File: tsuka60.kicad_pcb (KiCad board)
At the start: 2 copper layers, 285 x 95.1 mm, 166 parts, among them SW1 SW_Push, U1 ATmega32U4-AU, Y1 Resonator_Small

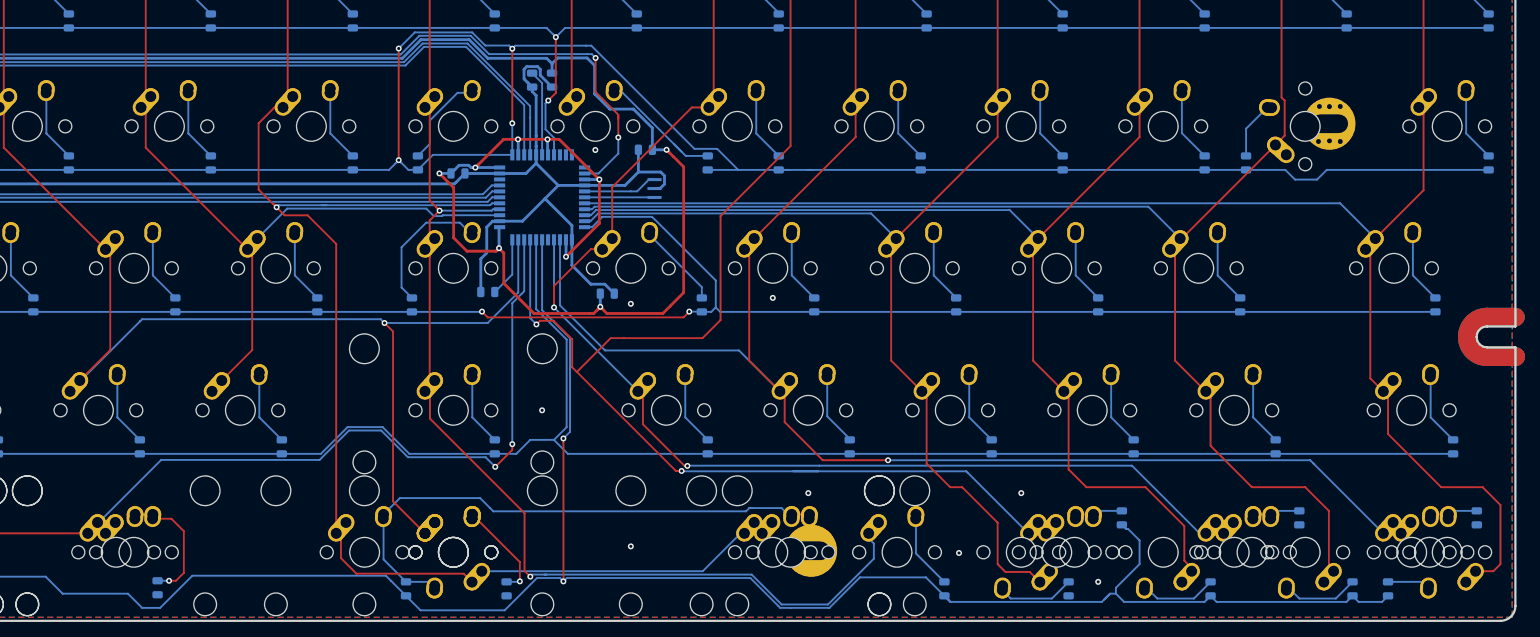
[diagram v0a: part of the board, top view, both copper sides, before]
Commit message: Fixed broken traces
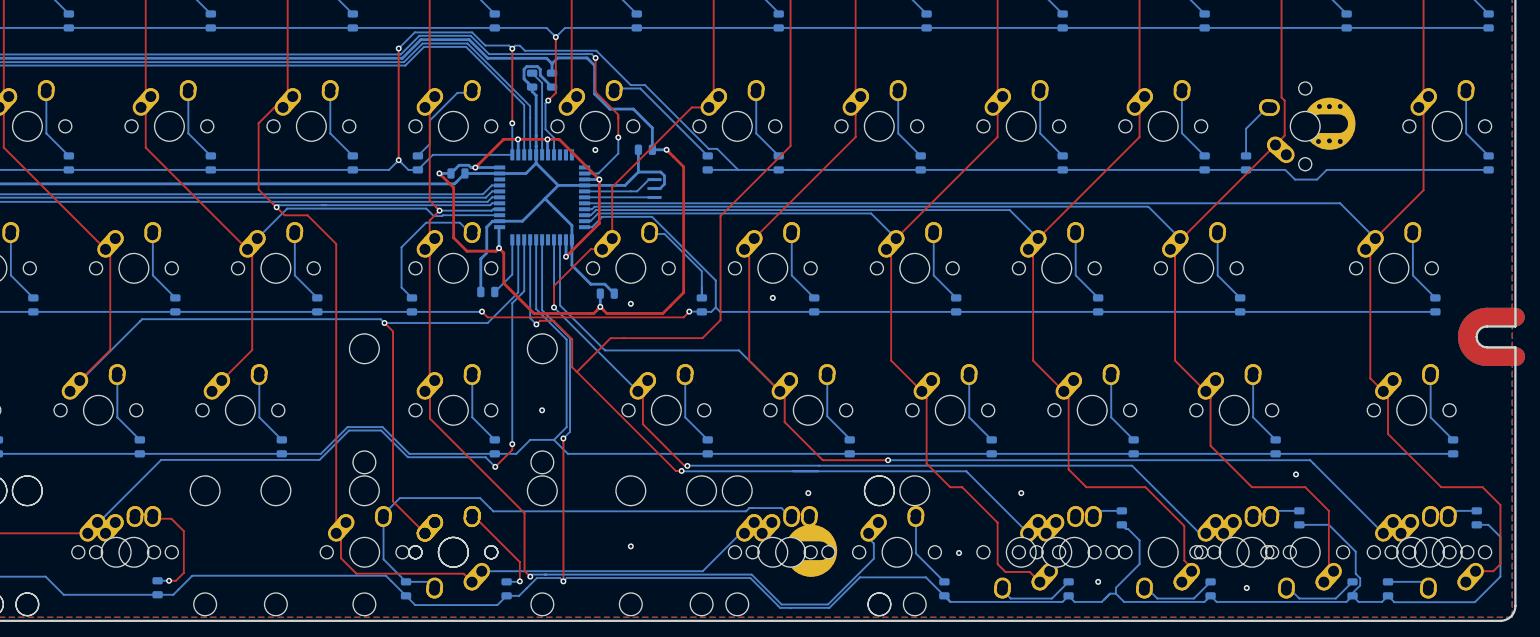
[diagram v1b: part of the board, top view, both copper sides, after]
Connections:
- D64 pad 1: Net-(D64-Pad1) -> Row4
- D65 pad 1: Net-(D65-Pad1) -> Row4
- D70 pad 1: Net-(D70-Pad1) -> Row4
- D71 pad 1: Net-(D71-Pad1) -> Row4
- D72 pad 1: Net-(D72-Pad1) -> Row4
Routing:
- net Row4: track 326.2 -> 366.5 mm
- net Net-(D40-Pad2): track 11.4 -> 14.3 mm
- net Net-(D24-Pad2): track 17.5 -> 16.6 mm
- net GND: vias 14 -> 16

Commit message: updated the schematic
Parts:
- added D52: D_Small, Diode_SMD:D_0805_2012Metric, B.Cu at (219.1, 183.5)
- added D54: D_Small, Diode_SMD:D_0805_2012Metric, B.Cu at (254.8, 183.5)
- added MX15-1: MX-LED, MX_Alps_Hybrid:MX-2U-NoLED, F.Cu at (361.2, 121.4)
- added MX31-1: MX-LED, MX_Alps_Hybrid:MX-1.25U-NoLED, F.Cu at (106.4, 159.5)
- added MX38-1: MX-LED, MX_Alps_Hybrid:MX-1U-NoLED, F.Cu at (242.1, 159.5)
- added MX52: MX-LED, MX_Alps_Hybrid:MX-1U-NoLED, F.Cu at (227.8, 178.6)
- added MX54: MX-LED, MX_Alps_Hybrid:MX-1U-NoLED, F.Cu at (246.9, 178.6)
- moved U1 23.8 mm to (225.4, 150.0)

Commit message: updated schematic and PCB
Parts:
- removed MX67: SPACE, MX_Alps_Hybrid:MX-7U-NoLED
- added D37: D_Small, Diode_SMD:D_0805_2012Metric, F.Cu at (175.6, 316.9)
- added D39: D_Small, Diode_SMD:D_0805_2012Metric, F.Cu at (180.0, 316.9)
- added D66: D_Small, Diode_SMD:D_0805_2012Metric, F.Cu at (184.5, 316.9)
- added MX37: LEGACY-H, MX_Alps_Hybrid:MX-1U-NoLED, F.Cu at (267.8, 305.3)
- added MX39: H, MX_Alps_Hybrid:MX-1U-NoLED, F.Cu at (188.2, 305.3)
- added MX44-1: RETURN-SHORT, MX_Alps_Hybrid:MX-1.25U-NoLED, F.Cu at (245.3, 305.3)
- added MX65: SPACE, MX_Alps_Hybrid:MX-7U-ReversedStabilizers-NoLED, F.Cu at (237.3, 197.6)
- added MX65-3: SPACE, MX_Alps_Hybrid:MX-6.25U-ReversedStabilizers-NoLED, F.Cu at (233.4, 264.2)
- added MX66-1: SPACE RIGHT, MX_Alps_Hybrid:MX-2.75U-ReversedStabilizers-NoLED, F.Cu at (258.4, 285.1)
- added MX66-2: SPACE RIGHT, MX_Alps_Hybrid:MX-3U-ReversedStabilizers-NoLED, F.Cu at (202.5, 285.1)
- added MX67-3: LEGACY-BOTTOM, MX_Alps_Hybrid:MX-1U-NoLED, F.Cu at (237.3, 197.6)
- MX1: value MX-LED -> ESC
- MX10: value MX-LED -> 7
- MX11: value MX-LED -> 8
- MX12: value MX-LED -> 9
- MX13: value MX-LED -> 10
- MX14: value MX-LED -> MINUS
- MX15: value MX-LED -> PLUS
- MX16: value MX-LED -> TAB 1
- MX17: value MX-LED -> TAB 2
- MX18: value MX-LED -> Q
- MX19: value MX-LED -> W
- MX2: value MX-LED -> TILDE
- MX20: value MX-LED -> E
- MX21: value MX-LED -> R
- MX22: value MX-LED -> T
- MX23: value MX-LED -> M4
- MX24: value MX-LED -> Y
- MX25: value MX-LED -> U
- MX26: value MX-LED -> I
- MX27: value MX-LED -> O
- MX28: value MX-LED -> P
- MX29: value MX-LED -> L-BRACKET
- MX3: value MX-LED -> 1
- MX30: value MX-LED -> R-BRACKET
- MX31: value MX-LED -> CAPS
- MX31-1: value MX-LED -> CAPS-SHORT
- MX32: value MX-LED -> A
- MX33: value MX-LED -> S
- MX34: value MX-LED -> D
- MX35: value MX-LED -> F
- MX36: value MX-LED -> G
- MX38: value MX-LED -> BACKSPACE
- MX4: value MX-LED -> 2
- MX40: value MX-LED -> J
- MX41: value MX-LED -> K
- MX42: value MX-LED -> L
- MX43: value MX-LED -> SEMI-COLON
- MX44: value MX-LED -> RETURN; footprint MX_Alps_Hybrid:MX-1U-NoLED -> MX_Alps_Hybrid:MX-1.75U-NoLED
- MX45: value MX-LED -> BACKSPACE 2U; footprint MX_Alps_Hybrid:MX-1.75U-NoLED -> MX_Alps_Hybrid:MX-2U-NoLED
- MX46: value MX-LED -> L-SHIFT
- MX47: value MX-LED -> Z
- MX48: value MX-LED -> X
- MX49: value MX-LED -> C
- MX5: value MX-LED -> 3
- MX50: value MX-LED -> V
- MX51: value MX-LED -> B
- MX52: value MX-LED -> M1
- MX53: value MX-LED -> M2
- MX54: value MX-LED -> M3
- MX55: value MX-LED -> N
- MX56: value MX-LED -> M
- MX57: value MX-LED -> COMMA
- MX58: value MX-LED -> STOP
- MX59: value MX-LED -> SLASH
- MX6: value MX-LED -> 4
- MX60: value MX-LED -> R-SHIFT
- MX64-1, MX64-2: value BACK SPACE -> SPACE LEFT
- MX65-1: footprint MX_Alps_Hybrid:MX-2U-ReversedStabilizers-NoLED -> MX_Alps_Hybrid:MX-2U-NoLED
- MX7: value MX-LED -> 5
- MX8: value MX-LED -> M5
- MX9: value MX-LED -> 6
- moved MX65-2 109.4 mm to (217.9, 305.3)
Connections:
- MX31-1 pad 1: Net-(D31-Pad2) -> Col0
- MX31-1 pad 2: Col0 -> Net-(D31-Pad2)

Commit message: updated the routing
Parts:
- removed D37, D68: D_Small, Diode_SMD:D_0805_2012Metric
- removed MX15-1: MX-LED, MX_Alps_Hybrid:MX-2U-NoLED
- removed MX38-1: MX-LED, MX_Alps_Hybrid:MX-1U-NoLED
- removed MX67-1: SPACE, MX_Alps_Hybrid:MX-2.75U-ReversedStabilizers-NoLED
- removed MX67-2: SPACE, MX_Alps_Hybrid:MX-3U-ReversedStabilizers-NoLED
- removed the MX67-3 at (225.4, 197.6)
- removed the MX67-3 at (237.3, 197.6)
- removed MX68-3: LEGACY, MX_Alps_Hybrid:MX-1.25U-NoLED
- added MX67-3: LEGACY-BOTTOM, MX_Alps_Hybrid:MX-1.25U-NoLED, F.Cu at (296.9, 197.6)
- D39, D66: moved to B.Cu
- MX65-1: footprint MX_Alps_Hybrid:MX-2U-NoLED -> MX_Alps_Hybrid:MX-2U-ReversedStabilizers-NoLED
- moved MX44-1 184.7 mm to (358.8, 159.5)
- moved D39 175.4 mm to (266.7, 164.4), turned to 90 degrees
- moved MX39 163.0 mm to (261.1, 159.5)
- moved D66 154.3 mm to (288.1, 202.6), turned to 90 degrees
- moved MX37 148.0 mm to (242.1, 159.5)
- moved Y1 134.8 mm to (130.8, 167.5)
- moved C2 133.8 mm to (130.8, 163.4), turned to 270 degrees
- moved C3 130.2 mm to (129.2, 182.1)
- moved C5 129.5 mm to (109.6, 163.7), turned to 180 degrees
- moved C4 128.4 mm to (124.2, 157.2)
- moved C1 128.3 mm to (121.7, 157.2)
- moved R4 128.3 mm to (114.3, 175.6), turned to 270 degrees
- moved MX66-2 117.0 mm to (280.2, 197.6)
- moved MX65-2 109.4 mm to (237.3, 197.6)
- moved U1 106.6 mm to (120.5, 168.8)
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- renumbered MX72 to MX72-4, MX73 to MX73-4, MX74 to MX74-4, MX75 to MX75-4
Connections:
- MX31-1 pad 1: Col0 -> Net-(D31-Pad2)
- MX31-1 pad 2: Net-(D31-Pad2) -> Col0
- MX37 pad 1: Col6 -> Col7
- MX37 pad 2: Net-(D37-Pad2) -> Net-(D38-Pad2)
- MX38 pad 1: Col7 -> Net-(D38-Pad2)
- MX38 pad 2: Net-(D38-Pad2) -> Col7
- MX44-1 pad 1: Col13 -> Net-(D44-Pad2)
- MX44-1 pad 2: Net-(D44-Pad2) -> Col13
- U1 pad 1: Row1 -> Row0
- U1 pad 10: Net-(U1-Pad10) -> Col1
- U1 pad 22: Row2 -> Net-(U1-Pad22)
- U1 pad 28: Row4 -> Col8
- U1 pad 29: Row3 -> Col7
- U1 pad 30: Col8 -> Col6
- U1 pad 31: Col3 -> Col5
- U1 pad 36: Col5 -> Net-(U1-Pad36)
- U1 pad 37: Col7 -> Row3
- U1 pad 38: Col6 -> Col3
- U1 pad 40: Col1 -> Row4
- U1 pad 8: Row0 -> Row1
- U1 pad 9: Net-(U1-Pad9) -> Row2
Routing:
- net GND: track 274.4 -> 74.1 mm, vias 16 -> 20
- net Col14: track 206.9 -> 384.3 mm
- net Net-(R1-Pad1): track 203.1 -> 26.1 mm, vias 4 -> 2
- net Col13: track 183.3 -> 359.8 mm, vias 0 -> 1
- net Col11: track 144.7 -> 300.1 mm
- net Col5: track 100.8 -> 254.4 mm
- net Col12: track 161.3 -> 314.4 mm
- net +5V: track 288.7 -> 138.1 mm, vias 9 -> 6
- net Col9: track 171.6 -> 322.1 mm
- net Col10: track 202.5 -> 341.2 mm, vias 1 -> 2
- net Col0: track 224.7 -> 104.5 mm, vias 0 -> 1
- net Net-(R3-Pad1): track 146.5 -> 37.1 mm
- net Net-(R2-Pad1): track 144.1 -> 38.8 mm
- net Col1: track 205.1 -> 110.4 mm
- net Col6: track 177.9 -> 267.4 mm, vias 1 -> 0
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
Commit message: fixed bug errors
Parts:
- moved R4 8.52 mm to (117.2, 183.6), turned to 90 degrees
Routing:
- net Row3: track 306.4 -> 328.3 mm
- net Col0: track 104.5 -> 93.4 mm
- net GND: track 74.1 -> 83.6 mm, vias 20 -> 21
- net Row4: track 347.8 -> 356.7 mm
- net Col3: track 200.3 -> 208.5 mm
- net Net-(R4-Pad2): track 3.34 -> 8.43 mm
- net Col2: track 176.0 -> 178.1 mm
- net +5V: track 138.1 -> 139.9 mm
- net Net-(D73-Pad2): track 82.7 -> 83.4 mm

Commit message: more improvements
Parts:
- moved SW1 4.95 mm to (122.9, 157.6)
- moved C1 4.60 mm to (121.7, 152.6)
- moved C4 4.60 mm to (124.2, 152.6)
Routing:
- net +5V: track 139.9 -> 147.6 mm
- net Net-(C1-Pad1): track 7.32 -> 12.3 mm
- net GND: track 83.6 -> 79.2 mm, vias 21 -> 26
- net Net-(D31-Pad2): track 47.2 -> 49.3 mm
- net Row1: track 291.7 -> 293.7 mm
- net Net-(R1-Pad1): track 26.1 -> 25.0 mm
- net Row2: track 262.7 -> 263.2 mm

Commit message: updated the pcb layout
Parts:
- moved C3 0.89 mm to (129.1, 183.0), turned to 90 degrees
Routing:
- net Col5: track 254.4 -> 759.1 mm
- net Col8: track 299.2 -> 308.7 mm
- net Col4: track 210.8 -> 215.7 mm
- net Net-(R2-Pad1): track 38.8 -> 36.6 mm
- net Net-(D31-Pad2): track 49.3 -> 47.2 mm
- net Col13: track 359.8 -> 361.5 mm
- net Net-(D62-Pad2): track 13.2 -> 14.8 mm
- net Col7: track 205.9 -> 207.3 mm
- net +5V: track 147.6 -> 146.2 mm
- net Col6: track 267.4 -> 268.6 mm
- net Net-(D72-Pad2): track 54.3 -> 55.4 mm
- net Col14: track 384.3 -> 385.4 mm
- net Row4: track 356.7 -> 357.7 mm
- net Net-(D65-Pad2): track 22.9 -> 23.8 mm
- net Net-(D73-Pad2): track 83.4 -> 84.3 mm
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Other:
- board text added: "Tsuka60 aka Semi Ergo Layout Prototype Two by RominRonin"
- board text removed: "Tsuka60 aka Semi Ergo Layout Prototype One by RominRonin"
